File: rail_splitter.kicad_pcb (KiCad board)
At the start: 2 copper layers, 100 x 86.5 mm, 90 parts, among them J1 input +, J2 input -, J3 +load, J4 gnd load, J5 -load, J6 shunt+ display pos, J7 shunt- display pos, J8 shunt+ display neg, J9 shunt- display neg, P1 PNP, Q1 PNP, Q10 PMOS, Q11 NMOS, Q12 NMOS, Q2 NPN, Q3 NPN, Q4 N, Q5 NPN, Q6 PNP, Q7 PMOS, Q8 NPN, Q9 PNP, SW1 SW_Push, SW3 SW_DPDT_x2, U1 OP07, U2 NE5532, U3 NE5532, U5 LM2936-3.3, U6 NE5532

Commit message: overa nova
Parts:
- removed C7: 100n, Capacitor_SMD:C_1206_3216Metric
- removed C7: 10n, Capacitor_SMD:C_1206_3216Metric
- removed the J6 at (60.5, 145.5)
- removed the J7 at (67.8, 145.2)
- removed the J7 at (35.4, 99.3)
- removed the J8 at (139.0, 145.8)
- removed the RV4 at (136.0, 120.4)
- added C9: 10n, Capacitor_SMD:C_1206_3216Metric, B.Cu at (136.8, 95.4)
- added J4: shunt- display neg, Connector_PinHeader_2.54mm:PinHeader_1x01_P2.54mm_Vertical, F.Cu at (102.8, 96.5)
- added J5: shunt+ display neg, Connector_PinHeader_2.54mm:PinHeader_1x01_P2.54mm_Vertical, F.Cu at (108.0, 98.5)
- added J7: shunt+ display pos, Connector_PinHeader_2.54mm:PinHeader_1x01_P2.54mm_Vertical, F.Cu at (94.0, 95.8)
- added RV3: R_Potentiometer, Potentiometer_SMD:Potentiometer_ACP_CA6-VSMD_Vertical, B.Cu at (65.0, 118.2)
- H1: renamed from H4; footprint MountingHole:MountingHole_2.1mm -> MountingHole:MountingHole_3.2mm_M3
- H2: renamed from H3; footprint MountingHole:MountingHole_2.1mm -> MountingHole:MountingHole_3.2mm_M3
- H3: renamed from H2; footprint MountingHole:MountingHole_2.1mm -> MountingHole:MountingHole_3.2mm_M3
- H4: renamed from H1; footprint MountingHole:MountingHole_2.1mm -> MountingHole:MountingHole_3.2mm_M3
- J9: value shunt- display neg -> shunt- display pos
- moved R1 89.3 mm to (66.0, 89.5)
- moved Q5 89.0 mm to (142.8, 138.2), turned to 0 degrees
- moved R18 88.9 mm to (141.3, 103.4)
- moved Q10 88.2 mm to (144.5, 104.5)
- moved Q9 88.2 mm to (144.5, 108.5)
- moved R20 88.2 mm to (140.3, 107.8)
- moved R2 87.4 mm to (69.6, 90.8), turned to -90 degrees
- moved R3 86.3 mm to (72.7, 90.8), turned to -90 degrees
- moved R4 85.3 mm to (64.8, 93.2), turned to 90 degrees
- moved Q4 85.3 mm to (138.8, 138.2), turned to 180 degrees
- moved C11 84.6 mm to (134.6, 103.4)
- moved R14 84.3 mm to (142.2, 134.0), turned to 90 degrees
- moved Q8 83.1 mm to (138.1, 103.4)
- moved SW2 82.1 mm to (144.0, 119.2), turned to 180 degrees
- moved C12 81.4 mm to (65.4, 139.1), turned to 180 degrees
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- renumbered C13 to C1, C9 to C10, C2 to C11, C5 to C12, C8 to C15, C10 to C16, C1 to C2, C6 to C3, C11 to C4, C3 to C5, C12 to C6, C4 to C8, D2 to D1, D1 to D2, D4 to D3, D7 to D4, D3 to D5, D5 to D6, J2 to J1, J1 to J2, J4 to J3, J5 to J6, J3 to J8, Q3 to Q10, Q10 to Q11, Q7 to Q12, Q4 to Q3, Q9 to Q4, Q8 to Q5, Q11 to Q6, Q12 to Q7, Q6 to Q8, Q5 to Q9, R36 to R1, R38 to R10, R1 to R11, R2 to R12, R18 to R13, R24 to R14, R19 to R15, R33 to R16, R16 to R17, R15 to R18, R20 to R19, R34 to R2, R14 to R20, R22 to R21, R21 to R22, R26 to R24, R13 to R25, R12 to R26, R17 to R27, R11 to R28, R9 to R29, R35 to R3, R10 to R30, R27 to R31, R8 to R32, R37 to R4, R4 to R5, R3 to R6, R5 to R7, R6 to R8, R7 to R9, RV2 to RV1, RV1 to RV2, RV3 to RV4, SW3 to SW1, SW1 to SW2, U6 to U2, U2 to U3, U5 to U4, U3 to U5
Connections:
- J6 pad 1: Net-(J5-Pin_1) (its old number) -> Net-(J4-Pin_1)
- J8 pad 1: Net-(J3-Pin_1) -> Net-(J8-Pin_1)
- J9 pad 1: Net-(J5-Pin_1) (its old number) -> Net-(J8-Pin_1)
- R19 pad 1: Net-(J5-Pin_1) (its old number) -> Net-(J4-Pin_1)
- R21 pad 1: Net-(J5-Pin_1) (its old number) -> Net-(J4-Pin_1)
- R25 pad 1: Net-(R13-Pad1) -> Net-(R25-Pad1)
- R26 pad 1: Net-(U2A--) (its old number) -> Net-(U5A--)
- R26 pad 2: Net-(U2B-+) (its old number) -> Net-(U5B-+)
- R28 pad 1: Net-(U2A-+) (its old number) -> Net-(U5A-+)
- R29 pad 2: Net-(U2A-+) (its old number) -> Net-(U5A-+)
- R30 pad 1: Net-(J3-Pin_1) -> Net-(J8-Pin_1)
- R30 pad 2: Net-(U2A--) (its old number) -> Net-(U5A--)
- R31 pad 2: Net-(R27-Pad2) -> Net-(R31-Pad2)
- R32 pad 2: Net-(J3-Pin_1) -> Net-(J8-Pin_1)
- U3 pad 1: Net-(U2B-+) (its old number) -> Net-(U3B--)
- U3 pad 2: Net-(U2A--) (its old number) -> Net-(U3A--)
- U3 pad 3: Net-(U2A-+) (its old number) -> Net-(U3A-+)
- U3 pad 5: Net-(U2B-+) (its old number) -> CURR_LIMIT
- U3 pad 6: CURR_LIMIT -> Net-(U3B--)
- U3 pad 7: Net-(R13-Pad1) -> Net-(R31-Pad2)
- U5 pad 1: Net-(U3B--) -> Net-(U5B-+)
- U5 pad 2: Net-(U3A--) -> Net-(U5A--)
- U5 pad 3: Net-(U3A-+) -> Net-(U5A-+)
- U5 pad 5: CURR_LIMIT -> Net-(U5B-+)
- U5 pad 6: Net-(U3B--) -> CURR_LIMIT
- U5 pad 7: Net-(R27-Pad2) -> Net-(R25-Pad1)
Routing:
- net Net-(J5-Pin_1) (its old number): track 133.5 -> 0.00 mm, vias 6 -> 0
- net Net-(Q4-C): track 131.0 -> 7.32 mm, vias 4 -> 0
- net GNDD: track 60.4 -> 176.6 mm, vias 0 -> 2
- net CURR_LIMIT: track 154.9 -> 54.6 mm, vias 2 -> 0
- net Net-(J4-Pin_1): track 0.00 -> 93.8 mm, vias 0 -> 2
- net Net-(J8-Pin_1): track 0.00 -> 92.7 mm, vias 0 -> 2
- net INPUT-: track 389.5 -> 300.0 mm, vias 12 -> 4
- net +3.3V: track 58.8 -> 131.0 mm, vias 0 -> 2
- net Net-(J3-Pin_1): track 71.8 -> 0.00 mm, vias 3 -> 0
- net INPUT+: track 391.7 -> 328.1 mm, vias 14 -> 6
- net Net-(D5-K): track 98.3 -> 36.1 mm, vias 1 -> 0
- net Net-(J7-Pin_1): track 125.3 -> 65.9 mm
- net enable+: track 65.2 -> 109.9 mm, vias 3 -> 2
- net /GND_SET: track 124.3 -> 80.9 mm
- net enable -: track 58.5 -> 87.9 mm, vias 2 -> 0
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
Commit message: overa opet
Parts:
- moved D5 83.7 mm to (56.8, 91.8)
- moved R25 81.2 mm to (58.2, 95.2), turned to 180 degrees
- moved C9 76.3 mm to (60.7, 91.5), turned to 180 degrees
- moved U5 68.4 mm to (64.7, 96.0), turned to 180 degrees
- moved C10 64.7 mm to (67.5, 101.8), turned to 90 degrees
- moved R26 61.3 mm to (68.2, 91.5), turned to 180 degrees
- moved R28 56.3 mm to (71.4, 100.0), turned to 0 degrees
- moved R29 55.2 mm to (71.5, 97.5), turned to 180 degrees
- moved R30 54.7 mm to (71.5, 94.8), turned to 180 degrees
- moved R22 19.0 mm to (125.2, 85.8), turned to 180 degrees
- moved C16 16.8 mm to (131.2, 86.0), turned to 180 degrees
- moved R10 16.7 mm to (57.9, 118.0)
- moved D6 15.2 mm to (140.2, 87.5)
- moved C15 15.2 mm to (134.7, 95.0)
- moved R21 15.2 mm to (123.7, 92.0)
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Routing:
- net CURR_LIMIT: track 54.6 -> 190.4 mm, vias 0 -> 4
- net Net-(D5-K): track 36.1 -> 136.2 mm
- net Net-(J7-Pin_1): track 65.9 -> 41.4 mm, vias 2 -> 1
- net Net-(U2B--): track 27.7 -> 49.7 mm, vias 0 -> 2
- net Net-(D3-A): track 8.54 -> 29.3 mm, vias 0 -> 1
- net Net-(J5-Pin_1): track 70.2 -> 54.4 mm
- net Net-(J4-Pin_1): track 93.8 -> 80.6 mm
- net Net-(J8-Pin_1): track 92.7 -> 79.8 mm
- net /GND_SET: track 80.9 -> 73.8 mm
- net Net-(U3A-+): track 12.9 -> 6.11 mm
- net INPUT+: track 328.1 -> 323.8 mm
- net Net-(P1-B): track 59.2 -> 55.7 mm, vias 3 -> 2
- net Net-(D3-K): track 6.67 -> 3.76 mm
- net INPUT-: track 300.0 -> 302.3 mm
- net enable+: track 109.9 -> 107.7 mm
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
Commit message: shunt fix
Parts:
- moved J4 21.7 mm to (124.2, 99.1)
- moved J5 12.6 mm to (120.6, 99.1)
- moved R19 1.40 mm to (106.6, 109.5)
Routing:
- net Net-(J4-Pin_1): track 80.6 -> 67.1 mm, vias 2 -> 1
- net Net-(J5-Pin_1): track 54.4 -> 44.6 mm, vias 2 -> 1
- net Net-(D5-K): track 136.2 -> 133.8 mm
- net GNDD: track 176.6 -> 174.8 mm
- net enable -: track 87.9 -> 86.8 mm
- net Net-(J7-Pin_1): track 41.4 -> 42.4 mm
- net INPUT-: track 302.3 -> 301.9 mm, vias 4 -> 2

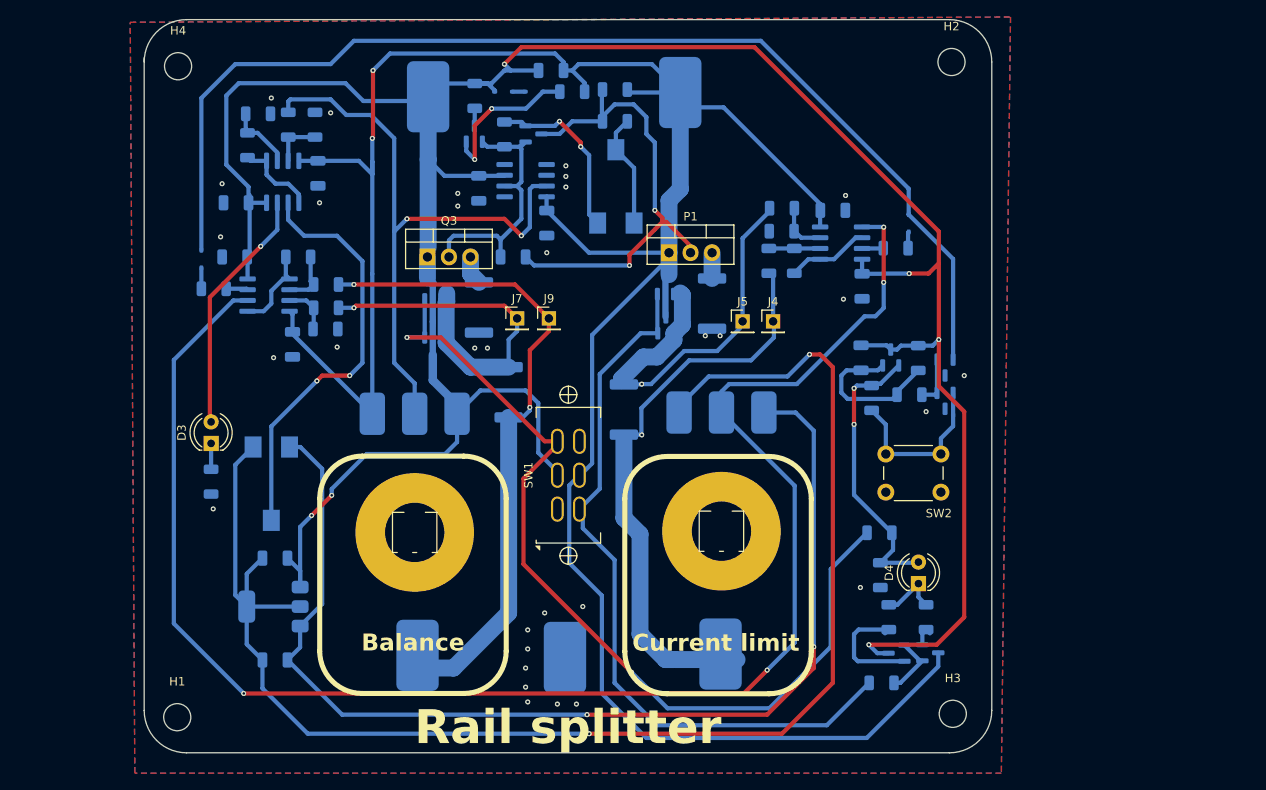
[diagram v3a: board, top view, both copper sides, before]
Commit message: moving block around
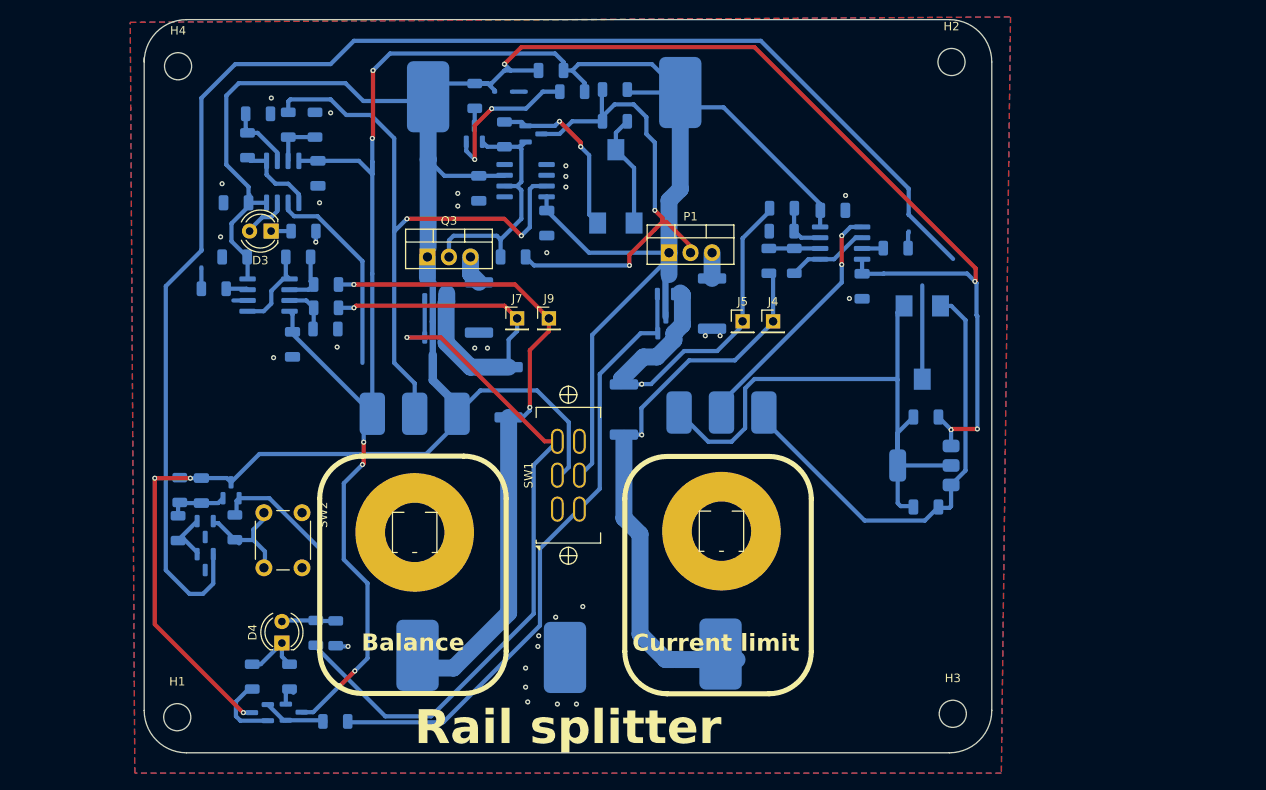
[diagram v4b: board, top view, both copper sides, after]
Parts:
- moved Q10 90.3 mm to (57.2, 127.5)
- moved Q9 88.6 mm to (57.2, 123.6)
- moved R18 88.5 mm to (54.2, 119.0)
- moved R20 87.7 mm to (54.0, 123.5), turned to -90 degrees
- moved Q8 79.4 mm to (60.2, 119.0)
- moved C11 79.4 mm to (56.8, 119.1)
- moved C12 78.9 mm to (142.2, 121.0)
- moved RV3 78.6 mm to (141.8, 101.6)
- moved U4 78.6 mm to (142.1, 116.1)
- moved C8 78.6 mm to (142.2, 110.4)
- moved R17 76.7 mm to (60.7, 123.4)
- moved D4 75.4 mm to (66.2, 137.1)
- moved Q4 75.4 mm to (63.6, 145.3)
- moved Q5 75.4 mm to (67.6, 145.2)
- moved R13 75.4 mm to (62.7, 141.0)
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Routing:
- net CURR_LIMIT: track 190.4 -> 31.3 mm, vias 4 -> 2
- net GNDD: track 174.8 -> 71.5 mm, vias 2 -> 0
- net +3.3V: track 131.0 -> 52.7 mm, vias 2 -> 0
- net Net-(D5-K): track 133.8 -> 172.2 mm
- net INPUT-: track 301.9 -> 268.9 mm, vias 2 -> 6
- net Net-(D3-A): track 29.3 -> 5.22 mm, vias 1 -> 0
- net enable+: track 107.7 -> 85.5 mm, vias 2 -> 1
- net Net-(U2B--): track 49.7 -> 35.2 mm, vias 2 -> 0
- net enable -: track 86.8 -> 73.3 mm
- net Net-(Q8-B): track 18.4 -> 5.91 mm
- net Net-(Q9-B): track 20.5 -> 13.6 mm
- net Net-(Q4-B): track 13.8 -> 7.70 mm
- net INPUT+: track 323.8 -> 328.7 mm, vias 6 -> 7
- net Net-(D4-A): track 34.0 -> 29.4 mm, vias 2 -> 0
- net GND: track 0.00 -> 2.76 mm, vias 32 -> 30
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
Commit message: cleared errors
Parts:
- moved RV3 71.1 mm to (71.0, 108.3), turned to 90 degrees
- moved C12 19.0 mm to (127.5, 109.0), turned to 90 degrees
- moved U4 12.0 mm to (132.4, 108.8), turned to 90 degrees
- moved C8 4.29 mm to (138.2, 109.0), turned to 90 degrees
- moved R20 3.34 mm to (56.6, 125.6)
- moved R18 3.06 mm to (56.6, 120.9)
- moved Q9 2.94 mm to (59.6, 125.3)
- moved Q10 2.94 mm to (59.6, 129.2)
- moved C11 2.90 mm to (59.0, 120.9)
- moved R17 2.90 mm to (62.7, 125.5)
- moved Q8 2.89 mm to (62.4, 120.9)
- moved C1 2.50 mm to (100.5, 69.5)
- moved SW2 2.37 mm to (71.0, 121.7)
- moved C10 2.30 mm to (66.0, 100.0), turned to 0 degrees
- moved H2 1.52 mm to (145.0, 70.0)
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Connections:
- C12 pad 2: GNDD -> GND
- C8 pad 2: GNDD -> GND
- RV3 pad 3: GNDD -> GND
- RV4 pad 3: GNDD -> GND
- U4 pad 2: GNDD -> GND
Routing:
- net CURR_LIMIT: track 31.3 -> 164.4 mm, vias 2 -> 4
- net +3.3V: track 52.7 -> 151.8 mm, vias 0 -> 2
- net GNDD: track 71.5 -> 0.00 mm
- net Net-(D5-K): track 172.2 -> 160.9 mm
- net Net-(J4-Pin_1): track 66.0 -> 55.7 mm
- net Net-(U2B--): track 35.2 -> 27.0 mm
- net Net-(D4-A): track 29.4 -> 21.5 mm, vias 0 -> 1
- net INPUT+: track 328.7 -> 324.3 mm, vias 7 -> 6
- net INPUT-: track 268.9 -> 265.7 mm
- net Net-(J8-Pin_1): track 79.8 -> 76.9 mm
- net GND: vias 30 -> 36
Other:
- board size 100 x 86.5 mm -> 100 x 85 mm

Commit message: rev
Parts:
- removed J4: shunt- display neg, Connector_PinHeader_2.54mm:PinHeader_1x01_P2.54mm_Vertical
- removed J5: shunt+ display neg, Connector_PinHeader_2.54mm:PinHeader_1x01_P2.54mm_Vertical
- removed J7: shunt+ display pos, Connector_PinHeader_2.54mm:PinHeader_1x01_P2.54mm_Vertical
- removed J9: shunt- display pos, Connector_PinHeader_2.54mm:PinHeader_1x01_P2.54mm_Vertical
- removed P1: PNP, Package_TO_SOT_THT:TO-220-3_Vertical
- removed Q1, Q4: PNP, Package_TO_SOT_SMD:SOT-23
- removed Q10, Q2, Q9: NPN, Package_TO_SOT_SMD:SOT-23
- removed R13, R14, R15: 1k, Resistor_SMD:R_1206_3216Metric
- added C17: 10n, Capacitor_SMD:C_1206_3216Metric, B.Cu at (109.5, 87.6)
- added D7: 1N4148WT, Diode_SMD:D_SOD-323, B.Cu at (110.6, 97.5)
- added Q13: BD909, Package_TO_SOT_THT:TO-220-3_Vertical, F.Cu at (72.5, 94.0)
- added Q14: BD910, Package_TO_SOT_THT:TO-220-3_Vertical, F.Cu at (122.5, 94.0)
- added Q15: MMBT5551L, Package_TO_SOT_SMD:SOT-23, B.Cu at (82.2, 91.4)
- added Q16: MMBT5551L, Package_TO_SOT_SMD:SOT-23, B.Cu at (103.2, 92.3)
- added Q17: MMBT5551L, Package_TO_SOT_SMD:SOT-23, B.Cu at (106.7, 92.3)
- Q11, Q12: value PMOS -> AO3401A
- Q3: value N -> MMBT5551L; footprint Package_TO_SOT_THT:TO-220-3_Vertical -> Package_TO_SOT_SMD:SOT-23; moved to B.Cu
- Q5: value NPN -> MMBT5551L
- Q6, Q7: value NMOS -> AO3400A
- Q8: value PNP -> MMBT5401
- moved SW2 72.0 mm to (142.9, 119.8)
- moved RV3 71.9 mm to (140.1, 88.3)
- moved D4 71.5 mm to (98.0, 73.0), turned to 180 degrees
- moved R1 63.9 mm to (127.3, 73.1)
- moved R4 63.9 mm to (126.0, 76.8)
- moved C3 63.9 mm to (124.7, 83.6)
- moved C4 63.9 mm to (134.4, 80.1)
- moved R2 63.9 mm to (130.9, 74.4)
- moved R3 63.9 mm to (134.0, 74.4)
- moved U2 63.9 mm to (130.2, 81.1)
- moved R20 63.2 mm to (107.1, 87.6)
- moved Q5 62.2 mm to (111.5, 101.1), turned to -90 degrees
- moved R16 61.7 mm to (114.6, 101.1), turned to -90 degrees
- moved R17 61.2 mm to (107.6, 83.9), turned to 0 degrees
- moved R18 56.6 mm to (103.4, 89.1), turned to 0 degrees
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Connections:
- D4 pad 2: Net-(D4-A) -> enable+
- J6 pad 1: Net-(J4-Pin_1) -> Net-(J6-Pin_1)
- Q11 pad 1: Net-(J7-Pin_1) -> enable+
- Q11 pad 2: enable+ -> Net-(Q11-S)
- Q12 pad 1: Net-(J7-Pin_1) -> enable+
- Q12 pad 2: enable+ -> Net-(Q11-S)
- Q3 pad 1: INPUT+ -> Net-(D2-K)
- Q3 pad 3: Net-(Q3-E) -> Net-(Q3-C)
- Q5 pad 1: Net-(Q4-C) -> Net-(D7-K)
- Q5 pad 2: Net-(Q5-B) -> INPUT-
- Q5 pad 3: INPUT- -> enable -
- Q6 pad 1: Net-(J5-Pin_1) -> enable -
- Q6 pad 2: enable - -> INPUT-
- Q6 pad 3: INPUT- -> Net-(Q6-D)
- Q7 pad 1: Net-(J5-Pin_1) -> enable -
- Q7 pad 2: enable - -> INPUT-
- Q7 pad 3: INPUT- -> Net-(Q6-D)
- Q8 pad 1: Net-(D4-A) -> Net-(Q8-B)
- Q8 pad 2: Net-(Q8-B) -> INPUT+
- Q8 pad 3: INPUT+ -> enable+
- R11 pad 1: Net-(Q3-E) -> Net-(Q13-E)
- R16 pad 1: Net-(Q4-C) -> INPUT+
- R17 pad 1: Net-(D4-A) -> Net-(D4-K)
- R19 pad 1: Net-(J4-Pin_1) -> Net-(J6-Pin_1)
- R19 pad 2: Net-(J5-Pin_1) -> Net-(Q6-D)
- R21 pad 1: Net-(J4-Pin_1) -> Net-(U3A--)
- R21 pad 2: Net-(U3A--) -> Net-(Q6-D)
- R22 pad 2: Net-(J5-Pin_1) -> Net-(J6-Pin_1)
- R24 pad 2: Net-(U3B--) -> Net-(U5A-+)
- R26 pad 1: Net-(U5A--) -> Net-(U3B--)
- R27 pad 1: enable+ -> INPUT-
- R27 pad 2: Net-(D4-A) -> enable+
- R28 pad 1: Net-(U5A-+) -> Net-(U3B-+)
- R29 pad 1: Net-(J7-Pin_1) -> Net-(Q11-S)
- R29 pad 2: Net-(U5A-+) -> Net-(U3B-+)
- R30 pad 2: Net-(U5A--) -> Net-(U3B--)
- R31 pad 1: Net-(D6-A) -> Net-(R31-Pad1)
- R31 pad 2: Net-(R31-Pad2) -> Net-(D6-A)
- R32 pad 1: Net-(J7-Pin_1) -> Net-(Q11-S)
- R6 pad 2: Net-(Q1-E) -> Net-(Q3-C)
- SW1 pad 4: unconnected-(SW1B-A-Pad4) -> enable -
- SW1 pad 6: enable - -> unconnected-(SW1B-C-Pad6)
- U3 pad 1: Net-(U3B--) -> Net-(U5A-+)
- U3 pad 5: CURR_LIMIT -> Net-(U3B-+)
- U3 pad 7: Net-(R31-Pad2) -> Net-(U5B-+)
- U5 pad 1: Net-(U5B-+) -> Net-(R31-Pad1)
- U5 pad 2: Net-(U5A--) -> CURR_LIMIT
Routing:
- net INPUT+: track 324.3 -> 94.1 mm, vias 6 -> 1
- net INPUT-: track 265.7 -> 54.8 mm, vias 6 -> 1
- net CURR_LIMIT: track 164.4 -> 5.48 mm, vias 4 -> 0
- net Net-(D5-K): track 160.9 -> 11.3 mm
- net +3.3V: track 151.8 -> 24.7 mm, vias 2 -> 0
- net Net-(J4-Pin_1): track 55.7 -> 0.00 mm, vias 1 -> 0
- net Net-(J5-Pin_1): track 44.6 -> 0.00 mm, vias 1 -> 0
- net Net-(J8-Pin_1): track 76.9 -> 32.9 mm, vias 2 -> 0
- net Net-(J7-Pin_1): track 42.4 -> 0.00 mm, vias 1 -> 0
- net enable -: track 73.3 -> 35.7 mm, vias 0 -> 2
- net Net-(J6-Pin_1): track 0.00 -> 34.2 mm, vias 0 -> 1
- net Net-(D4-K): track 7.40 -> 36.0 mm
- net Net-(D3-A): track 5.22 -> 29.9 mm, vias 0 -> 2
- net Net-(D4-A): track 21.5 -> 0.00 mm, vias 1 -> 0
- net /GND_SET: track 73.8 -> 94.8 mm, vias 2 -> 4
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
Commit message: rev_2
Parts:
- moved R10 40.6 mm to (133.1, 97.5), turned to 180 degrees
- moved D3 38.4 mm to (134.5, 93.5), turned to 180 degrees
- moved D4 10.0 mm to (108.0, 73.2)
- moved R12 3.10 mm to (128.2, 100.0), turned to 90 degrees
- moved C1 1.25 mm to (94.5, 76.4)
- moved D1 1.25 mm to (90.5, 78.8)
- moved D2 1.25 mm to (93.8, 78.8)
- moved R5 1.25 mm to (97.8, 78.8)
- moved C15 0.60 mm to (94.0, 108.0)
- moved C6 0.55 mm to (97.5, 91.2)
- moved R30 0.50 mm to (91.5, 113.1)
- moved C12 0.45 mm to (140.8, 106.2)
- moved C9 0.25 mm to (100.9, 98.2)
- moved R6 0.20 mm to (92.3, 81.0)
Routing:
- net INPUT-: track 54.8 -> 274.8 mm, vias 1 -> 8
- net INPUT+: track 94.1 -> 300.8 mm, vias 1 -> 8
- net Net-(Q17-B): track 11.3 -> 69.5 mm, vias 0 -> 2
- net Net-(R8-Pad1): track 8.65 -> 39.5 mm, vias 0 -> 2
- net CURR_LIMIT: track 5.48 -> 31.7 mm, vias 0 -> 2
- net Net-(D3-A): track 29.9 -> 11.9 mm, vias 2 -> 1
- net Net-(D4-K): track 36.0 -> 32.4 mm
- net Net-(U5A-+): track 11.2 -> 13.2 mm
- net /GND_SET: track 94.8 -> 96.7 mm, vias 4 -> 2
- net enable+: track 82.0 -> 80.4 mm
- net enable -: track 35.7 -> 37.2 mm, vias 2 -> 3
- net Net-(D3-K): track 2.90 -> 4.03 mm
- net Net-(U5B-+): track 17.0 -> 18.1 mm
- net Net-(Q14-E): track 3.72 -> 3.19 mm
- net Net-(J6-Pin_1): vias 1 -> 0
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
